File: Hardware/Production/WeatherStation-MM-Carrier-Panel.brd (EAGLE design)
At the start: 162.8 x 131.1 mm, 615 parts, among them J11 microSD, J13 RJ11 - WIND, J15 MICROMOD-2222-C, J16 QWIIC_RIGHT_ANGLE, J17 JTAG, J19 microSD, J2 JTAG, J24 RJ11 - RAIN, J25 RJ11 - WIND, J26 MICROMOD-2222-C, J3 QWIIC_RIGHT_ANGLE, J30 QWIIC_RIGHT_ANGLE, J31 JTAG, J33 microSD, J38 RJ11 - RAIN, J39 RJ11 - WIND, J40 MICROMOD-2222-C, J44 QWIIC_RIGHT_ANGLE, J45 JTAG, J47 microSD, J52 RJ11 - RAIN, J53 RJ11 - WIND, J54 MICROMOD-2222-C, J7 RJ11 - RAIN, U1 BME280, U10 BME280, U11 VEML6075, U12 AS3935, U13 AP7361C-33FGE, U14 BME280, U15 VEML6075, U16 AS3935, U2 VEML6075, U3 AS3935, U4 AP7361C-33FGE, U5 AP7361C-33FGE, U6 BME280, U7 VEML6075, U8 AS3935, U9 AP7361C-33FGE

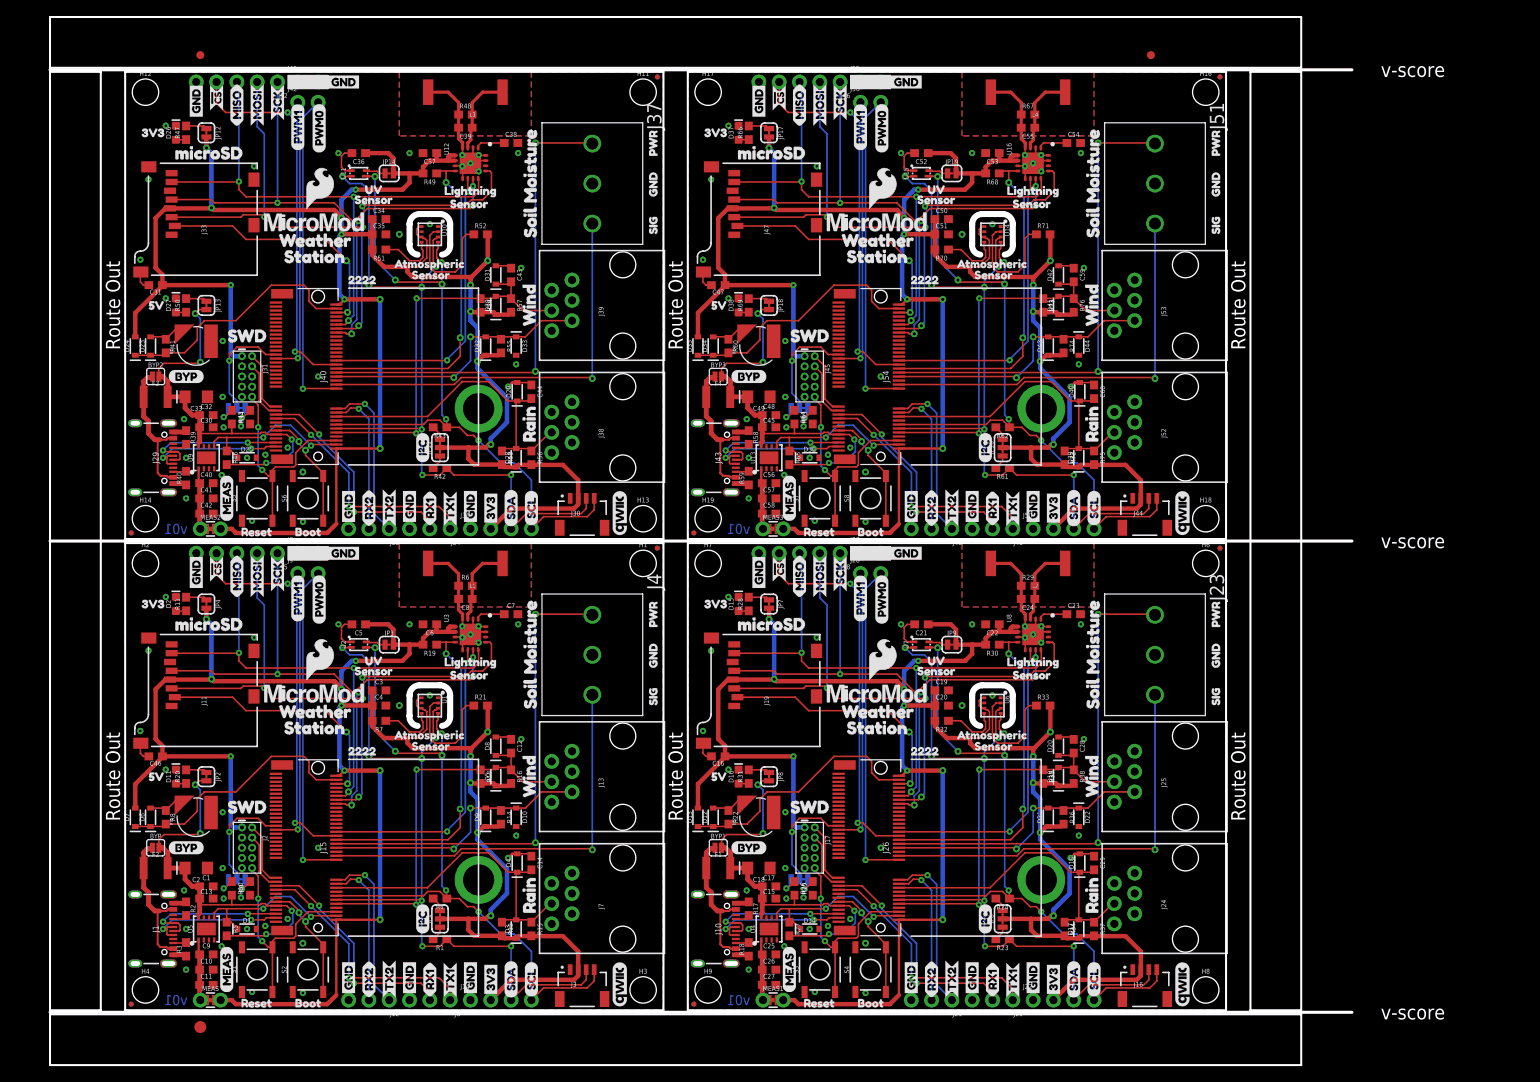
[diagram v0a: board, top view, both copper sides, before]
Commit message: Moved 3.3V LED circuit to match 5V. Re-panelized and re-cammed
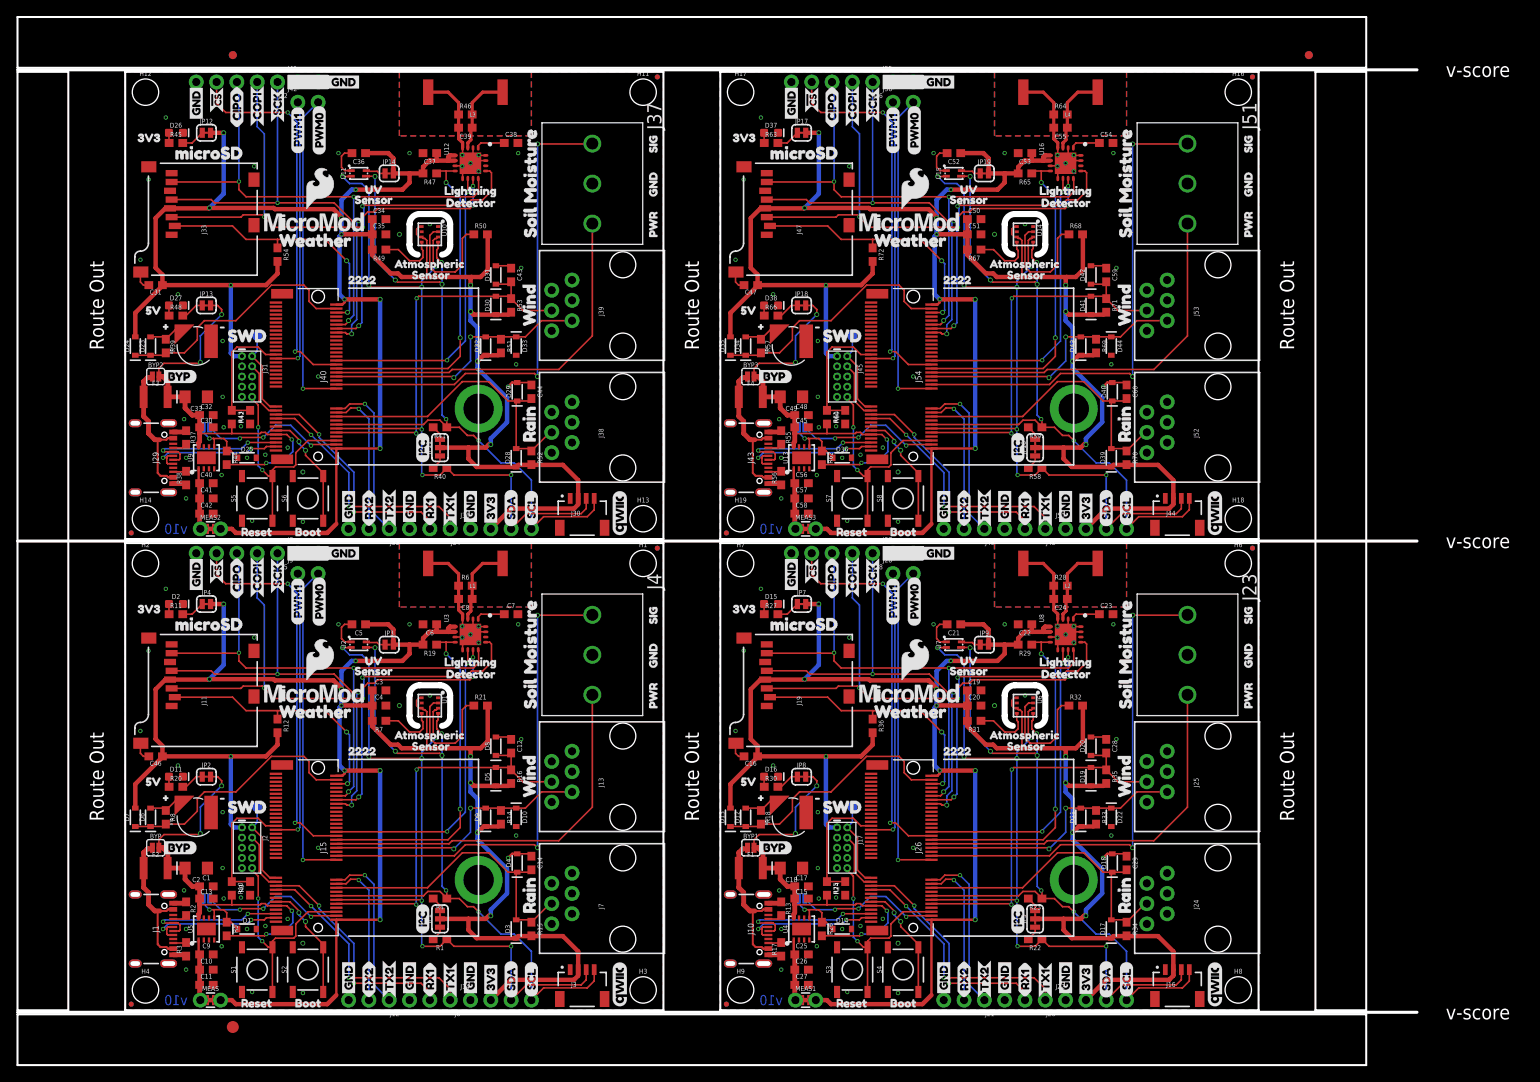
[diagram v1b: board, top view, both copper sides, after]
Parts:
- removed R73, R74: 10k, SparkFun-Resistors:0603
- removed R75, R76: 100k, SparkFun-Resistors:0603
- added E$4: (no value), SparkFun-Aesthetics:FIDUCIAL-1X2
- added E$5: (no value), SparkFun-Retired:FIDUCIAL-1.5X3
- added TP1, TP2, TP3, TP4: TEST-POINT3X5, SparkFun-Connectors:PAD.03X.05
- added U$265: (no value), buzzard_labels (3):PWR2
- added U$266: (no value), buzzard_labels (3):GND0
- added U$267: (no value), buzzard_labels (3):SIG1
- added U$268, U$269: (no value), buzzard_labels (9):COPI0
- added U$270: (no value), buzzard_labels (10):#0
- added U$271: (no value), buzzard_labels (10):#1
- added U$272: (no value), buzzard_labels (10):DETECTOR2
- added U$273: (no value), buzzard_labels (11):BYP0
- added U$274, U$275: (no value), buzzard_labels (12):CIPO0
- added U$276: (no value), buzzard_labels (76):VE0
- E$3: device SparkFun-Retired:FIDUCIAL-1.5X3 -> SparkFun-Aesthetics:FIDUCIAL-1X2
- JP10, JP15, JP20: value VIN/3 -> VE; device SparkFun-Jumpers:SMT-JUMPER_3_2-NC_TRACE_SILK -> SparkFun-Jumpers:SMT-JUMPER_2_NO_SILK
- JP5: value VIN/3 -> (none)
- JP6: value (none) -> VE; device SparkFun-Jumpers:SMT-JUMPER_3_2-NC_TRACE_SILK -> SparkFun-Jumpers:SMT-JUMPER_2_NO_SILK
- R12, R36, R44, R54, R72: value 10k -> 100k
- R13, R55: value 10k -> 5.1k
- R15, R16: value 100k -> 43k
- R18, R39: value 5.1k -> 3.3k
- R22, R41: value 1k -> 2.2k
- R24, R42: value 2.2k -> 10k
- R25: value 10k -> 20k
- R26: value 20k -> 100k
- R27: value 100k -> 1k
- R28, R31, R47, R50, R60, R69: value 1k -> 10k
- R30, R48, R63: value 10k -> 1k
- R34, R35, R52, R53, R70, R71: value 10k -> 43k
- R37, R38, R56: value 100k -> 5.1k
- R40, R58, R59: value 5.1k -> 2.2k
- R43, R61: value 2.2k -> 20k
- R45: value 20k -> 1k
- R46, R65: value 100k -> 10k
- R57: value 100k -> 3.3k
- R62: value 2.2k -> 100k
- R64: value 20k -> 10k
- R8: value 1k -> 3.3k
- U$101: device SparkFun-Buzzard:GND_P -> buzzard_labels (12):RX25
- U$102: device buzzard_labels (10):PWM10 -> buzzard_labels (12):TX24
- U$103, U$172: device buzzard_labels (12):RX25 -> buzzard_labels (12):TX24
- U$104, U$170: device buzzard_labels (12):TX24 -> buzzard_labels (12):RX25
- U$105: device buzzard_labels (12):TX24 -> buzzard_labels (1):PWM01
- U$106: device buzzard_labels (12):RX25 -> buzzard_labels (1):PWM01
- U$107: device buzzard_labels (1):PWM01 -> buzzard_labels:LIGHTNING8
- U$108: device buzzard_labels (1):PWM01 -> buzzard_labels:SENSOR7
- U$109: device buzzard_labels:LIGHTNING8 -> buzzard_labels:UV6
- U$110: device buzzard_labels:SENSOR7 -> buzzard_labels (2):RAIN1
- U$111: device buzzard_labels:SENSOR7 -> buzzard_labels (2):SOIL_MOISTURE2
- U$112: device buzzard_labels:UV6 -> buzzard_labels (2):WIND0
- U$113: device buzzard_labels (2):RAIN1 -> buzzard_labels (3):GND0
- U$114: device buzzard_labels (2):SOIL_MOISTURE2 -> buzzard_labels (3):PWR2
- U$115: device buzzard_labels (2):WIND0 -> buzzard_labels (3):SIG1
- U$116: device buzzard_labels (3):GND0 -> buzzard_labels (3):WEATHER4
- U$117: device buzzard_labels (3):PWR2 -> buzzard_labels (4):MICROSD0
- U$118: device buzzard_labels (3):SIG1 -> buzzard_labels (4):SWD1
- U$119: device buzzard_labels (3):WEATHER4 -> buzzard_labels (5):3V31
- U$120: device buzzard_labels (3):STATION5 -> buzzard_labels (5):5V0
- U$121: device buzzard_labels (4):MICROSD0 -> SparkFun-Aesthetics:SFE_LOGO_FLAME_.2
- U$122, U$254: device buzzard_labels (4):SWD1 -> buzzard_labels (3):WEATHER4
- U$123: device buzzard_labels (5):3V31 -> buzzard_labels (73):ATMOSPHERIC0
- U$124: device buzzard_labels (5):5V0 -> buzzard_labels (73):SENSOR1
- U$125: device buzzard_labels (6):VIN#30 -> SparkFun-MicroMod:MICROMOD_LOGO_.5
- U$126: device SparkFun-Aesthetics:SFE_LOGO_FLAME_.2 -> SparkFun-MicroMod:MICROMOD_LOGO_.5
- U$127: device buzzard_labels (3):WEATHER4 -> buzzard_labels (3):PWR2
- U$128: device buzzard_labels (3):STATION5 -> buzzard_labels (3):GND0
- U$129: device buzzard_labels (73):ATMOSPHERIC0 -> buzzard_labels (3):SIG1
- U$130: device buzzard_labels (73):SENSOR1 -> buzzard_labels (9):COPI0
- U$131: device SparkFun-MicroMod:MICROMOD_LOGO_.5 -> buzzard_labels (9):COPI0
- U$132: device SparkFun-MicroMod:MICROMOD_LOGO_.5 -> buzzard_labels (10):#0
- U$133: device buzzard_labels (9):RESET3 -> buzzard_labels (10):#1
- U$134: device SparkFun-Buzzard:MEAS -> buzzard_labels (10):DETECTOR2
- U$135: device SparkFun-Buzzard:MOSI_O -> buzzard_labels (11):BYP0
- U$136: device SparkFun-Buzzard:MISO_I -> buzzard_labels (12):CIPO0
- U$137: device SparkFun-Buzzard:SCK_O -> buzzard_labels (12):CIPO0
- U$138: device SparkFun-Buzzard:!CS_O -> buzzard_labels (76):VE0
- U$139: device SparkFun-Buzzard:GND_P -> buzzard_labels (9):RESET3
- U$14: device buzzard_labels (9):RESET3 -> buzzard_labels (11):BYP0
- U$140: device SparkFun-Buzzard:GND_P -> SparkFun-Buzzard:MEAS
- U$141: device buzzard_labels (10):BOOT2 -> SparkFun-Buzzard:SCK_O
- U$142: device SparkFun-Buzzard:BYP -> SparkFun-Buzzard:!CS_O
- U$143: device buzzard_labels (6):RX10 -> SparkFun-Buzzard:GND_P
- U$144, U$220: device buzzard_labels (6):TX13 -> SparkFun-Buzzard:GND_P
- U$145, U$214: device SparkFun-Buzzard:GND_P -> buzzard_labels (10):BOOT2
- U$146, U$156: device SparkFun-Buzzard:GND_P -> buzzard_labels (6):RX10
- U$147: device SparkFun-Buzzard:I2C -> buzzard_labels (6):TX13
- U$149: device SparkFun-Buzzard:3V3_P -> SparkFun-Buzzard:GND_P
- U$150: device SparkFun-Buzzard:SDA_IO -> SparkFun-Buzzard:I2C
- U$151, U$159, U$217: device SparkFun-Buzzard:SCL_IO -> SparkFun-Buzzard:GND_P
- U$152, U$221: device SparkFun-Buzzard:GND_P -> SparkFun-Buzzard:3V3_P
- U$153: device buzzard_labels (6):RX10 -> SparkFun-Buzzard:SDA_IO
- U$154: device buzzard_labels (6):TX13 -> SparkFun-Buzzard:SCL_IO
- U$157: device SparkFun-Buzzard:3V3_P -> buzzard_labels (6):TX13
- U$158, U$224: device SparkFun-Buzzard:SDA_IO -> SparkFun-Buzzard:GND_P
- U$160: device SparkFun-Buzzard:SCK_O -> SparkFun-Buzzard:3V3_P
- U$161: device SparkFun-Buzzard:MOSI_O -> SparkFun-Buzzard:SDA_IO
- U$162: device SparkFun-Buzzard:MISO_I -> SparkFun-Buzzard:SCL_IO
- U$163, U$72: device SparkFun-Buzzard:!CS_O -> SparkFun-Buzzard:SCK_O
- U$164, U$211, U$233, U$73: device SparkFun-Buzzard:GND_P -> SparkFun-Buzzard:!CS_O
- U$165, U$99: device buzzard_labels (9):22229 -> SparkFun-Buzzard:GND_P
- U$166: device buzzard_labels (10):PWM10 -> buzzard_labels (9):22229
- U$167, U$98: device SparkFun-Buzzard:GND_P -> buzzard_labels (10):PWM10
- U$168, U$234: device buzzard_labels (10):PWM10 -> SparkFun-Buzzard:GND_P
- U$169, U$238: device buzzard_labels (12):RX25 -> buzzard_labels (10):PWM10
- U$173, U$239: device buzzard_labels (1):PWM01 -> buzzard_labels (12):RX25
- U$175: device buzzard_labels:LIGHTNING8 -> buzzard_labels (1):PWM01
- U$176: device buzzard_labels:SENSOR7 -> buzzard_labels:LIGHTNING8
- U$186: device buzzard_labels (3):STATION5 -> buzzard_labels (4):MICROSD0
- U$187: device buzzard_labels (4):MICROSD0 -> buzzard_labels (4):SWD1
- U$188: device buzzard_labels (4):SWD1 -> buzzard_labels (5):3V31
- U$189: device buzzard_labels (5):3V31 -> buzzard_labels (5):5V0
- U$190: device buzzard_labels (5):5V0 -> SparkFun-Aesthetics:SFE_LOGO_FLAME_.2
- U$191: device buzzard_labels (6):VIN#30 -> buzzard_labels (3):WEATHER4
- U$192: device SparkFun-Aesthetics:SFE_LOGO_FLAME_.2 -> buzzard_labels (73):ATMOSPHERIC0
- U$193: device buzzard_labels (3):WEATHER4 -> buzzard_labels (73):SENSOR1
- U$194: device buzzard_labels (3):STATION5 -> SparkFun-MicroMod:MICROMOD_LOGO_.5
- U$195: device buzzard_labels (73):ATMOSPHERIC0 -> SparkFun-MicroMod:MICROMOD_LOGO_.5
- U$196: device buzzard_labels (73):SENSOR1 -> buzzard_labels (3):PWR2
- U$197: device SparkFun-MicroMod:MICROMOD_LOGO_.5 -> buzzard_labels (3):GND0
- U$198: device SparkFun-MicroMod:MICROMOD_LOGO_.5 -> buzzard_labels (3):SIG1
- U$199: device buzzard_labels (9):RESET3 -> buzzard_labels (9):COPI0
- U$200: device SparkFun-Buzzard:MEAS -> buzzard_labels (9):COPI0
- U$201, U$69: device SparkFun-Buzzard:MOSI_O -> buzzard_labels (10):#0
- U$202, U$70: device SparkFun-Buzzard:MISO_I -> buzzard_labels (10):#1
- U$203, U$71: device SparkFun-Buzzard:SCK_O -> buzzard_labels (10):DETECTOR2
- U$204: device SparkFun-Buzzard:!CS_O -> buzzard_labels (11):BYP0
- U$205, U$206: device SparkFun-Buzzard:GND_P -> buzzard_labels (12):CIPO0
- U$207: device buzzard_labels (10):BOOT2 -> buzzard_labels (76):VE0
- U$208: device SparkFun-Buzzard:BYP -> buzzard_labels (9):RESET3
- U$209: device buzzard_labels (6):RX10 -> SparkFun-Buzzard:MEAS
- U$21: device buzzard_labels (6):VIN#30 -> buzzard_labels (76):VE0
- U$210: device buzzard_labels (6):TX13 -> SparkFun-Buzzard:SCK_O
- U$213: device SparkFun-Buzzard:I2C -> SparkFun-Buzzard:GND_P
- U$215: device SparkFun-Buzzard:3V3_P -> buzzard_labels (6):RX10
- U$216: device SparkFun-Buzzard:SDA_IO -> buzzard_labels (6):TX13
- U$219: device buzzard_labels (6):RX10 -> SparkFun-Buzzard:I2C
- U$222, U$230: device SparkFun-Buzzard:GND_P -> SparkFun-Buzzard:SDA_IO
- U$223: device SparkFun-Buzzard:3V3_P -> SparkFun-Buzzard:SCL_IO
- U$225: device SparkFun-Buzzard:SCL_IO -> buzzard_labels (6):RX10
- U$226: device SparkFun-Buzzard:SCK_O -> buzzard_labels (6):TX13
- U$227: device SparkFun-Buzzard:MOSI_O -> SparkFun-Buzzard:GND_P
- U$228, U$96: device SparkFun-Buzzard:MISO_I -> SparkFun-Buzzard:GND_P
- U$229: device SparkFun-Buzzard:!CS_O -> SparkFun-Buzzard:3V3_P
- U$231: device buzzard_labels (9):22229 -> SparkFun-Buzzard:SCL_IO
- U$232: device buzzard_labels (10):PWM10 -> SparkFun-Buzzard:SCK_O
- U$235: device buzzard_labels (12):RX25 -> buzzard_labels (9):22229
- U$236: device buzzard_labels (12):TX24 -> buzzard_labels (10):PWM10
- U$237: device buzzard_labels (12):TX24 -> SparkFun-Buzzard:GND_P
- U$24, U$252: device buzzard_labels (3):STATION5 -> buzzard_labels (3):PWR2
- U$240: device buzzard_labels (1):PWM01 -> buzzard_labels (12):TX24
- U$241: device buzzard_labels:LIGHTNING8 -> buzzard_labels (12):TX24
- U$242: device buzzard_labels:SENSOR7 -> buzzard_labels (12):RX25
- U$243: device buzzard_labels:SENSOR7 -> buzzard_labels (1):PWM01
- U$244: device buzzard_labels:UV6 -> buzzard_labels (1):PWM01
- U$245: device buzzard_labels (2):RAIN1 -> buzzard_labels:LIGHTNING8
- U$246: device buzzard_labels (2):SOIL_MOISTURE2 -> buzzard_labels:SENSOR7
- U$247: device buzzard_labels (2):WIND0 -> buzzard_labels:UV6
- U$248: device buzzard_labels (3):GND0 -> buzzard_labels (2):RAIN1
- U$249: device buzzard_labels (3):PWR2 -> buzzard_labels (2):SOIL_MOISTURE2
- U$250: device buzzard_labels (3):SIG1 -> buzzard_labels (2):WIND0
- U$251: device buzzard_labels (3):WEATHER4 -> buzzard_labels (3):GND0
- U$253: device buzzard_labels (4):MICROSD0 -> buzzard_labels (3):SIG1
- U$255: device buzzard_labels (5):3V31 -> buzzard_labels (4):MICROSD0
- U$256: device buzzard_labels (5):5V0 -> buzzard_labels (4):SWD1
- U$257: device buzzard_labels (6):VIN#30 -> buzzard_labels (5):3V31
- U$258: device SparkFun-Aesthetics:SFE_LOGO_FLAME_.2 -> buzzard_labels (5):5V0
- U$259: device buzzard_labels (3):WEATHER4 -> SparkFun-Aesthetics:SFE_LOGO_FLAME_.2
- U$26: device buzzard_labels:SENSOR7 -> buzzard_labels (9):RESET3
- U$260: device buzzard_labels (3):STATION5 -> buzzard_labels (3):WEATHER4
- U$27: device SparkFun-Buzzard:BYP -> buzzard_labels (12):CIPO0
- U$50: device SparkFun-Buzzard:MOSI_O -> buzzard_labels (12):CIPO0
- U$51: device SparkFun-Buzzard:MISO_I -> SparkFun-Buzzard:MEAS
- U$57: device SparkFun-Buzzard:MEAS -> buzzard_labels (3):GND0
- U$63: device buzzard_labels (3):STATION5 -> buzzard_labels (3):SIG1
- U$7: device SparkFun-Buzzard:MOSI_O -> buzzard_labels (9):COPI0
- U$75: device buzzard_labels (10):BOOT2 -> SparkFun-Buzzard:GND_P
- U$76: device SparkFun-Buzzard:BYP -> buzzard_labels (10):BOOT2
- U$8: device SparkFun-Buzzard:MISO_I -> buzzard_labels (9):COPI0
- U$95: device SparkFun-Buzzard:MOSI_O -> SparkFun-Buzzard:!CS_O
- U$97: device SparkFun-Buzzard:!CS_O -> buzzard_labels (9):22229
- U13, U4, U5, U9: value AP7361C-33FGE -> AP7361C-33FGEUDFN-8; device ublox:8-UDFN -> SparkFun-IC-Power:UDFN-8
- moved E$3 184.4 mm to (148.0, 119.4)
- moved R37 129.1 mm to (7.62, 71.6)
- moved U$138 122.2 mm to (83.9, 14.0), flipped to the bottom, turned to 0 degrees
- moved R38 117.1 mm to (7.62, 66.5), turned to 90 degrees
- moved E$2 114.8 mm to (13.5, 119.4), flipped to the bottom
- moved U$135 109.6 mm to (78.9, 20.3), turned to 0 degrees
- moved U$134 102.7 mm to (113.7, 42.0), turned to 0 degrees
- moved JP5 99.9 mm to (113.8, 11.4), flipped to the top, turned to 90 degrees
- moved JP6 99.6 mm to (10.2, 14.0), flipped to the bottom, turned to 0 degrees
- moved U$136 95.0 mm to (88.4, 51.4)
- moved U$137 91.5 mm to (88.4, 51.6), flipped to the bottom
- moved U$51 88.2 mm to (88.0, 3.68), turned to 0 degrees
- moved U$201 86.7 mm to (3.81, 85.6), turned to 0 degrees
- moved U$69 86.7 mm to (3.81, 26.7), turned to 0 degrees
- moved U$206 86.3 mm to (14.0, 110.5), turned to 90 degrees
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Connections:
- removed net N$20 (its old number): JP6.3, R24.2
- removed net N$23 (its old number): JP7.1, R28.2
- removed net N$28 (its old number): R33.1, U6.2
- removed net N$34 (its old number): J29.B5, R40.2
- removed net N$37 (its old number): JP11.1, R42.2
- removed net N$42 (its old number): JP13.1, R50.2
- removed net N$48 (its old number): JP15.1, R44.2
- removed net N$51 (its old number): BT4.+, D34.A, R60.1
- removed net N$56 (its old number): D37.A, R66.1
- removed net N$58: JP18.1, R69.2
- removed net N$59: D38.A, R69.1
- removed net N$60: R71.1, U14.2
- removed net N$61: R70.1, U14.5
- removed net N$63: JP20.3, R64.1
- removed net N$64: JP20.1, R63.2
- removed net SPI_MISO: J11.DO, J15.64, J5.3, U3.12
- removed net SPI_MISO1: J18.3, J19.DO, J26.64, U8.12
- removed net SPI_MISO2: J32.3, J33.DO, J40.64, U12.12
- removed net SPI_MISO3: J46.3, J47.DO, J54.64, U16.12
- removed net SPI_MOSI: J11.DI, J15.62, J5.2, U3.13
- removed net SPI_MOSI1: J18.2, J19.DI, J26.62, U8.13
- removed net SPI_MOSI2: J32.2, J33.DI, J40.62, U12.13
- removed net SPI_MOSI3: J46.2, J47.DI, J54.62, U16.13
- new net N$22: D15.A, R27.1
- new net N$25: D16.A, R30.1
- new net N$30: J29.B5, R38.2
- new net N$38: JP13.1, R48.2
- new net N$41: R49.1, U10.5
- new net N$46: JP16.3, R59.2
- new net N$54: R68.1, U14.2
- new net SPI_CIPO: J11.DO/DAT0, J15.64, J5.3, U3.12
- new net SPI_CIPO1: J18.3, J19.DO/DAT0, J26.64, U8.12
- new net SPI_CIPO2: J32.3, J33.DO/DAT0, J40.64, U12.12
- new net SPI_CIPO3: J46.3, J47.DO/DAT0, J54.64, U16.12
- new net SPI_COPI: J11.DI/CMD, J15.62, J5.2, U3.13
- new net SPI_COPI1: J18.2, J19.DI/CMD, J26.62, U8.13
- new net SPI_COPI2: J32.2, J33.DI/CMD, J40.62, U12.13
- new net SPI_COPI3: J46.2, J47.DI/CMD, J54.62, U16.13
- new net VREG_EN: D1.C, JP6.2, R5.1, U5.5
- new net VREG_EN1: D14.C, JP10.2, R26.1, U4.5
- new net VREG_EN2: D25.C, JP15.2, R44.1, U9.5
- new net VREG_EN3: D36.C, JP20.2, R62.1, U13.5
- net 3.3V: no longer R13.2
- net 3.3V1: now also JP5.2, R29.2, R31.2; no longer JP6.2, R30.2, R37.2, R38.2
- net 3.3V2: now also R47.2, R50.2; no longer R55.2, R56.2, R57.2
- net 3.3V3: now also R65.2, R67.2, R69.2; no longer R73.2, R74.2, R75.2, R76.2
- net 3.3V_EN: now also JP6.1; no longer D1.C, R5.1, U5.5
- net 3.3V_EN1: now also JP10.1; no longer D14.C, R27.1, U4.5
- net 3.3V_EN2: now also JP15.1; no longer D25.C, R46.1, U9.5
- net 3.3V_EN3: now also JP20.1; no longer D36.C, R65.1, U13.5
- net GND1: now also R13.1, R24.1, R28.1; no longer R18.1, R25.1, R29.1
- net GND2: now also R37.1, R38.1, R42.1, R46.1; no longer R39.1, R40.1, R44.1, R48.1
- net GND3: now also R55.1, R56.1, R60.1, R64.1; no longer R58.1, R59.1, R63.1, R67.1
- net I2C_SCL1: now also R23.1; no longer R24.1
- net I2C_SCL2: now also R41.1; no longer R43.1
- net I2C_SCL3: now also R59.1; no longer R62.1
- net I2C_SDA1: now also R22.1; no longer R23.1
- net I2C_SDA2: now also R40.1; no longer R42.1
- net I2C_SDA3: now also R58.1; no longer R61.1
- net INP1: now also R28.2; no longer R29.2
- net INP2: now also R46.2; no longer R48.2
- net INP3: now also R64.2; no longer R67.2
- net LIGHTNING_!CS!1: now also R29.1; no longer R30.1
- net LIGHTNING_!CS!2: now also R47.1; no longer R49.1
- net LIGHTNING_!CS!3: now also R65.1; no longer R68.1
- net N$12: now also J10.B5, R17.2; no longer JP5.1, R9.2
- net N$13: now also BT2.+, D12.A, R18.1; no longer J10.A5, R17.2
- net N$17: now also JP5.3, R23.2; no longer J10.B5, R18.2
- net N$18: now also JP5.1, R22.2; no longer BT2.+, D12.A, R22.1
- net N$21: now also JP7.1, R27.2; no longer JP6.1, R23.2
- net N$24: now also JP8.1, R30.2; no longer D15.A, R28.1
- net N$26: now also R32.1, U6.2; no longer JP8.1, R31.2
- net N$27: now also U6.5; no longer D16.A
- net N$29: now also J29.A5, R37.2; no longer R32.1, U6.5
- net N$31: now also BT3.+, D23.A, R39.1; no longer JP10.3, R26.1
- net N$32: now also JP11.3, R41.2; no longer JP10.1, R25.2
- net N$33: now also JP11.1, R40.2; no longer J29.A5, R39.2
- net N$35: now also JP12.1, R45.2; no longer BT3.+, D23.A, R41.1
- net N$36: now also D26.A, R45.1; no longer JP11.3, R43.2
- net N$39: now also D27.A, R48.1; no longer JP12.1, R47.2
- net N$40: now also R50.1, U10.2; no longer D26.A, R47.1
- net N$43: now also J43.A5, R55.2; no longer D27.A, R50.1
- net N$44: now also J43.B5, R56.2; no longer R52.1, U10.2
- net N$45: now also BT4.+, D34.A, R57.1; no longer R51.1, U10.5
- net N$47: now also JP16.1, R58.2; no longer JP15.3, R45.1
- net N$49: now also JP17.1, R63.2; no longer J43.A5, R58.2
- net N$50: now also D37.A, R63.1; no longer J43.B5, R59.2
- net N$52: now also JP18.1, R66.2; no longer JP16.3, R62.2
- net N$53: now also D38.A, R66.1; no longer JP16.1, R61.2
- net N$55: now also R67.1, U14.5; no longer JP17.1, R66.2
- net N$9: now also J10.A5, R13.2; no longer JP5.3, R10.1
- net RAIN: no longer R12.1
- net RAIN1: no longer R37.1
- net RAIN2: now also R52.1; no longer R53.1, R56.1
- net RAIN3: now also R70.1; no longer R72.1, R75.1
- net RTC_3V1: now also R18.2; no longer R22.2
- net RTC_3V2: now also R39.2; no longer R41.2
- net RTC_3V3: now also R57.2; no longer R60.2
- net SD_!CS!: now also J11.CS/DAT3, R12.1; no longer J11.CS
- net SD_!CS!1: now also J19.CS/DAT3, R36.1; no longer J19.CS
- net SD_!CS!2: now also J33.CS/DAT3, R54.1; no longer J33.CS
- net SD_!CS!3: now also J47.CS/DAT3, R72.1; no longer J47.CS
- net SOIL_MOIST_PWR: now also J4.3; no longer J4.1
- net SOIL_MOIST_PWR1: now also J23.3; no longer J23.1
- net SOIL_MOIST_PWR2: now also J37.3; no longer J37.1
- net SOIL_MOIST_PWR3: now also J51.3; no longer J51.1
- net SOIL_MOIST_SIG: now also J4.1; no longer J4.3
- net SOIL_MOIST_SIG1: now also J23.1; no longer J23.3
- net SOIL_MOIST_SIG2: now also J37.1; no longer J37.3
- net SOIL_MOIST_SIG3: now also J51.1; no longer J51.3
- net SWDIO: now also TP1.P$1
- net SWDIO1: now also TP2.P$1
- net SWDIO2: now also TP3.P$1
- net SWDIO3: now also TP4.P$1
- net VIN/1: now also R24.2, R25.1; no longer JP10.2
- net VIN/2: now also R42.2, R43.1; no longer JP15.2
- net VIN/3: now also R10.1, R9.2; no longer JP5.2
- net VIN/4: now also R60.2, R61.1; no longer JP20.2
- net VIN1: now also R25.2; no longer R27.2
- net VIN2: now also R43.2, R44.2; no longer R45.2, R46.2
- net VIN3: now also R61.2, R62.2; no longer R64.2, R65.2
- net WDIR1: now also R33.1; no longer R36.1
- net WDIR2: now also R51.1; no longer R55.1
- net WDIR3: now also R69.1; no longer R74.1
- net WSPEED: no longer R13.1
- net WSPEED1: no longer R38.1
- net WSPEED2: now also R53.1; no longer R54.1, R57.1
- net WSPEED3: now also R71.1; no longer R73.1, R76.1
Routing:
- net SPI_MOSI3: track 80.2 -> 0.00 mm, vias 4 -> 0
- net SPI_MOSI1: track 80.2 -> 0.00 mm, vias 4 -> 0
- net SPI_COPI1: track 0.00 -> 80.2 mm, vias 0 -> 4
- net SPI_MOSI: track 80.2 -> 0.00 mm, vias 4 -> 0
- net SPI_COPI: track 0.00 -> 80.2 mm, vias 0 -> 4
- net SPI_MOSI2: track 80.2 -> 0.00 mm, vias 4 -> 0
- net SPI_COPI3: track 0.00 -> 80.2 mm, vias 0 -> 4
- net SPI_COPI2: track 0.00 -> 80.2 mm, vias 0 -> 4
- net SPI_MISO3: track 71.8 -> 0.00 mm, vias 3 -> 0
- net SPI_MISO2: track 71.8 -> 0.00 mm, vias 3 -> 0
- net SPI_MISO1: track 71.8 -> 0.00 mm, vias 3 -> 0
- net SPI_CIPO3: track 0.00 -> 71.8 mm, vias 0 -> 3
- net SPI_CIPO2: track 0.00 -> 71.8 mm, vias 0 -> 3
- net SPI_CIPO1: track 0.00 -> 71.8 mm, vias 0 -> 3
- net SPI_MISO: track 71.8 -> 0.00 mm, vias 3 -> 0
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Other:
- board size 162.8 x 131.1 mm -> 175 x 131.1 mm
- board text added: "ROUTE OUT"
- board text added: "v10"
- board text removed: "v01"

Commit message: Updated M.2 connector with increased tCream layer. Regenerated production files
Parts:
- R19, R29, R47, R65: value 10k -> 100k
- moved E$5 24.4 mm to (-9.23, 6.86)
- moved E$1 22.9 mm to (-9.23, 116.3)
- moved E$2 22.9 mm to (-9.23, 116.3)
- moved E$3 4.33 mm to (151.0, 116.3)
- moved E$4 4.33 mm to (151.0, 116.3)
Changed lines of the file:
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@@
 <attribute name="VALUE" x="42.545" y="52.324" size="0.6096" layer="27" font="vector" ratio="20" align="top-center"/>
 </element>
-<element name="R19" library="SparkFun-Resistors" package="0603" value="10k" x="38.1" y="45.72" smashed="yes" rot="R180">
+<element name="R19" library="SparkFun-Resistors" package="0603" value="100k" x="38.1" y="45.72" smashed="yes" rot="R180">
 <attribute name="NAME" x="38.1" y="44.958" size="0.6096" layer="25" font="vector" ratio="20" rot="R180" align="bottom-center"/>
-<attribute name="PROD_ID" value="RES-00824" x="38.1" y="45.72" size="1.778" layer="27" font="vector" ratio="15" rot="R180" display="off"/>
-<attribute name="VALUE" x="38.1" y="46.482" size="0.6096" layer="27" font="vector" ratio="20" rot="R180" align="top-center"/>
+<attribute name="PROD_ID" value="RES-07828" x="38.1" y="45.72" size="1.778" layer="27" font="vector" ratio="15" rot="R180" display="off"/>
+<attribute name="VALUE" value="100k" x="38.1" y="46.482" size="0.6096" layer="27" font="vector" ratio="20" rot="R180" align="top-center"/>
 </element>
 <element name="L1" library="SparkFun-Coils" package="MA5532-AE" value="100uH" x="42.545" y="55.88" smashed="yes" rot="R180">
@@
 <attribute name="VALUE" x="116.967" y="52.324" size="0.6096" layer="27" font="vector" ratio="20" align="top-center"/>
 </element>
-<element name="R29" library="SparkFun-Resistors" package="0603" value="10k" x="112.522" y="45.72" smashed="yes" rot="R180">
+<element name="R29" library="SparkFun-Resistors" package="0603" value="100k" x="112.522" y="45.72" smashed="yes" rot="R180">
 <attribute name="NAME" x="112.522" y="44.958" size="0.6096" layer="25" font="vector" ratio="20" rot="R180" align="bottom-center"/>
-<attribute name="PROD_ID" value="RES-00824" x="112.522" y="45.72" size="1.778" layer="27" font="vector" ratio="15" rot="R180" display="off"/>
-<attribute name="VALUE" x="112.522" y="46.482" size="0.6096" layer="27" font="vector" ratio="20" rot="R180" align="top-center"/>
+<attribute name="PROD_ID" value="RES-07828" x="112.522" y="45.72" size="1.778" layer="27" font="vector" ratio="15" rot="R180" display="off"/>
+<attribute name="VALUE" value="100k" x="112.522" y="46.482" size="0.6096" layer="27" font="vector" ratio="20" rot="R180" align="top-center"/>
 </element>
 <element name="L2" library="SparkFun-Coils" package="MA5532-AE" value="100uH" x="116.967" y="55.88" smashed="yes" rot="R180">
@@
 <attribute name="VALUE" x="42.545" y="111.252" size="0.6096" layer="27" font="vector" ratio="20" align="top-center"/>
 </element>
-<element name="R47" library="SparkFun-Resistors" package="0603" value="10k" x="38.1" y="104.648" smashed="yes" rot="R180">
+<element name="R47" library="SparkFun-Resistors" package="0603" value="100k" x="38.1" y="104.648" smashed="yes" rot="R180">
 <attribute name="NAME" x="38.1" y="103.886" size="0.6096" layer="25" font="vector" ratio="20" rot="R180" align="bottom-center"/>
-<attribute name="PROD_ID" value="RES-00824" x="38.1" y="104.648" size="1.778" layer="27" font="vector" ratio="15" rot="R180" display="off"/>
-<attribute name="VALUE" x="38.1" y="105.41" size="0.6096" layer="27" font="vector" ratio="20" rot="R180" align="top-center"/>
+<attribute name="PROD_ID" value="RES-07828" x="38.1" y="104.648" size="1.778" layer="27" font="vector" ratio="15" rot="R180" display="off"/>
+<attribute name="VALUE" value="100k" x="38.1" y="105.41" size="0.6096" layer="27" font="vector" ratio="20" rot="R180" align="top-center"/>
 </element>
 <element name="L3" library="SparkFun-Coils" package="MA5532-AE" value="100uH" x="42.545" y="114.808" smashed="yes" rot="R180">
@@
 <attribute name="VALUE" x="116.967" y="111.252" size="0.6096" layer="27" font="vector" ratio="20" align="top-center"/>
 </element>
-<element name="R65" library="SparkFun-Resistors" package="0603" value="10k" x="112.522" y="104.648" smashed="yes" rot="R180">
+<element name="R65" library="SparkFun-Resistors" package="0603" value="100k" x="112.522" y="104.648" smashed="yes" rot="R180">
 <attribute name="NAME" x="112.522" y="103.886" size="0.6096" layer="25" font="vector" ratio="20" rot="R180" align="bottom-center"/>
-<attribute name="PROD_ID" value="RES-00824" x="112.522" y="104.648" size="1.778" layer="27" font="vector" ratio="15" rot="R180" display="off"/>
-<attribute name="VALUE" x="112.522" y="105.41" size="0.6096" layer="27" font="vector" ratio="20" rot="R180" align="top-center"/>
+<attribute name="PROD_ID" value="RES-07828" x="112.522" y="104.648" size="1.778" layer="27" font="vector" ratio="15" rot="R180" display="off"/>
+<attribute name="VALUE" value="100k" x="112.522" y="105.41" size="0.6096" layer="27" font="vector" ratio="20" rot="R180" align="top-center"/>
 </element>
 <element name="L4" library="SparkFun-Coils" package="MA5532-AE" value="100uH" x="116.967" y="114.808" smashed="yes" rot="R180">
@@
 <attribute name="VALUE" x="92.71" y="94.488" size="0.6096" layer="27" font="vector" ratio="20" rot="R270" align="top-center"/>
 </element>
-<element name="E$1" library="SparkFun-Aesthetics" package="FIDUCIAL-1X2" value="" x="13.462" y="119.4435" smashed="yes"/>
-<element name="E$2" library="SparkFun-Aesthetics" package="FIDUCIAL-1X2" value="" x="13.462" y="119.4435" smashed="yes" rot="MR0"/>
-<element name="E$3" library="SparkFun-Aesthetics" package="FIDUCIAL-1X2" value="" x="148.0185" y="119.4435" smashed="yes"/>
-<element name="E$4" library="SparkFun-Aesthetics" package="FIDUCIAL-1X2" value="" x="148.0185" y="119.4435" smashed="yes" rot="MR0"/>
-<element name="E$5" library="SparkFun-Retired" package="FIDUCIAL-1.5X3" value="" x="13.462" y="-2.0955" smashed="yes"/>
+<element name="E$1" library="SparkFun-Aesthetics" package="FIDUCIAL-1X2" value="" x="-9.22781875" y="116.2685" smashed="yes"/>
+<element name="E$2" library="SparkFun-Aesthetics" package="FIDUCIAL-1X2" value="" x="-9.22781875" y="116.2685" smashed="yes" rot="MR0"/>
+<element name="E$3" library="SparkFun-Aesthetics" package="FIDUCIAL-1X2" value="" x="150.95981875" y="116.2685" smashed="yes"/>
+<element name="E$4" library="SparkFun-Aesthetics" package="FIDUCIAL-1X2" value="" x="150.95981875" y="116.2685" smashed="yes" rot="MR0"/>
+<element name="E$5" library="SparkFun-Retired" package="FIDUCIAL-1.5X3" value="" x="-9.22781875" y="6.858" smashed="yes"/>
 </elements>
 <signals>
